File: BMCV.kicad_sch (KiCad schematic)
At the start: 30 parts, among them J13 DebugPins, J14 USB_C_Receptacle_USB2.0_14P, J17 ExpanderPort, SW14 Reset, SW15 Boot, U32 TXS0108EPW, U36 STM32G474CETx, Y1 38.4MHz 10pF

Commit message: rename symbol & footprint libs
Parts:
- J14: footprint MyParts:GT-USB-7035E -> BMCV:GT-USB-7035E
- SW14, SW15: footprint MyParts:TS-1095PS-AXXBX-C3DX -> BMCV:TS-1095PS-AXXBX-C3DX
- VR1: footprint MyParts:PTL6015xxxxxxx -> BMCV:PTL6015xxxxxxx; symbol MySymbols:PTLxx-xxxx-xxxxx -> BMCV:PTLxx-xxxx-xxxxx
- Z1: footprint MyParts:CataclystPanel -> BMCV:CataclystPanel; symbol MySymbols:FrontPanel -> BMCV:FrontPanel
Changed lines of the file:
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@@
 			)
 		)
-		(property "Footprint" "MyParts:TS-1095PS-AXXBX-C3DX"
+		(property "Footprint" "BMCV:TS-1095PS-AXXBX-C3DX"
 			(at 227.33 86.36 0)
 			(effects
@@
 	)
 	(symbol
-		(lib_id "MySymbols:PTLxx-xxxx-xxxxx")
+		(lib_id "BMCV:PTLxx-xxxx-xxxxx")
 		(at 59.69 189.23 0)
 		(unit 1)
@@
 			)
 		)
-		(property "Footprint" "MyParts:PTL6015xxxxxxx"
+		(property "Footprint" "BMCV:PTL6015xxxxxxx"
 			(at 88.9 284.15 0)
 			(effects
@@
 	)
 	(symbol
-		(lib_id "MySymbols:FrontPanel")
+		(lib_id "BMCV:FrontPanel")
 		(at 93.98 49.53 0)
 		(unit 1)
@@
 			)
 		)
-		(property "Footprint" "MyParts:CataclystPanel"
+		(property "Footprint" "BMCV:CataclystPanel"
 			(at 95.25 48.895 0)
 			(effects
@@
 			)
 		)
-		(property "Footprint" "MyParts:GT-USB-7035E"
+		(property "Footprint" "BMCV:GT-USB-7035E"
 			(at 41.91 102.87 0)
 			(effects
@@
 			)
 		)
-		(property "Footprint" "MyParts:TS-1095PS-AXXBX-C3DX"
+		(property "Footprint" "BMCV:TS-1095PS-AXXBX-C3DX"
 			(at 242.57 119.38 0)
 			(effects

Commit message: clea up project
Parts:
- Z1: footprint BMCV:CataclystPanel -> BMCV:BMCVPanel
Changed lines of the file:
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@@
 		)
 		(instances
-			(project "cataclyst"
+			(project "BMCV"
 				(path "/9b519346-c6ba-4bde-a176-1e9938a671fb"
 					(reference "C2")
@@
 		)
 		(instances
-			(project "cataclyst"
+			(project "BMCV"
 				(path "/9b519346-c6ba-4bde-a176-1e9938a671fb"
 					(reference "C6")
@@
 		)
 		(instances
-			(project "cataclyst"
+			(project "BMCV"
 				(path "/9b519346-c6ba-4bde-a176-1e9938a671fb"
 					(reference "C5")
@@
 		)
 		(instances
-			(project "cataclyst"
+			(project "BMCV"
 				(path "/9b519346-c6ba-4bde-a176-1e9938a671fb"
 					(reference "#PWR08")
@@
 		)
 		(instances
-			(project "cataclyst"
+			(project "BMCV"
 				(path "/9b519346-c6ba-4bde-a176-1e9938a671fb"
 					(reference "#PWR013")
@@
 		)
 		(instances
-			(project "cataclyst"
+			(project "BMCV"
 				(path "/9b519346-c6ba-4bde-a176-1e9938a671fb"
 					(reference "C46")
@@
 		)
 		(instances
-			(project "cataclyst"
+			(project "BMCV"
 				(path "/9b519346-c6ba-4bde-a176-1e9938a671fb"
 					(reference "#PWR0282")
@@
 		)
 		(instances
-			(project "cataclyst"
+			(project "BMCV"
 				(path "/9b519346-c6ba-4bde-a176-1e9938a671fb"
 					(reference "#PWR06")
@@
 		)
 		(instances
-			(project "cataclyst"
+			(project "BMCV"
 				(path "/9b519346-c6ba-4bde-a176-1e9938a671fb"
 					(reference "#PWR0284")
@@
 		)
 		(instances
-			(project "cataclyst"
+			(project "BMCV"
 				(path "/9b519346-c6ba-4bde-a176-1e9938a671fb"
 					(reference "#PWR029")
@@
 		)
 		(instances
-			(project "cataclyst"
+			(project "BMCV"
 				(path "/9b519346-c6ba-4bde-a176-1e9938a671fb"
 					(reference "C94")
@@
 			)
 		)
-		(property "Footprint" "BMCV:CataclystPanel"
+		(property "Footprint" "BMCV:BMCVPanel"
 			(at 95.25 48.895 0)
 			(effects
@@
 		)
 		(instances
-			(project "cataclyst"
+			(project "BMCV"
 				(path "/9b519346-c6ba-4bde-a176-1e9938a671fb"
 					(reference "#PWR030")
@@
 		)
 		(instances
-			(project "cataclyst"
+			(project "BMCV"
 				(path "/9b519346-c6ba-4bde-a176-1e9938a671fb"
 					(reference "#PWR0285")
@@
 		)
 		(instances
-			(project "cataclyst"
+			(project "BMCV"
 				(path "/9b519346-c6ba-4bde-a176-1e9938a671fb"
 					(reference "R163")
@@
 		)
 		(instances
-			(project "cataclyst"
+			(project "BMCV"
 				(path "/9b519346-c6ba-4bde-a176-1e9938a671fb"
 					(reference "C4")
@@
 		)
 		(instances
-			(project "cataclyst"
+			(project "BMCV"
 				(path "/9b519346-c6ba-4bde-a176-1e9938a671fb"
 					(reference "C7")
@@
 		)
 		(instances
-			(project "cataclyst"
+			(project "BMCV"
 				(path "/9b519346-c6ba-4bde-a176-1e9938a671fb"
 					(reference "R159")
@@
 		)
 		(instances
-			(project "cataclyst"
+			(project "BMCV"
 				(path "/9b519346-c6ba-4bde-a176-1e9938a671fb"
 					(reference "R2")
@@
 		)
 		(instances
-			(project "cataclyst"
+			(project "BMCV"
 				(path "/9b519346-c6ba-4bde-a176-1e9938a671fb"
 					(reference "C3")
@@
 		)
 		(instances
-			(project "cataclyst"
+			(project "BMCV"
 				(path "/9b519346-c6ba-4bde-a176-1e9938a671fb"
 					(reference "C93")
@@
 		)
 		(instances
-			(project "cataclyst"
+			(project "BMCV"
 				(path "/9b519346-c6ba-4bde-a176-1e9938a671fb"
 					(reference "R41")
@@
 		)
 		(instances
-			(project "cataclyst"
+			(project "BMCV"
 				(path "/9b519346-c6ba-4bde-a176-1e9938a671fb"
 					(reference "#PWR07")
@@
 		)
 		(instances
-			(project "cataclyst"
+			(project "BMCV"
 				(path "/9b519346-c6ba-4bde-a176-1e9938a671fb"
 					(reference "R162")
@@
 		)
 		(instances
-			(project "cataclyst"
+			(project "BMCV"
 				(path "/9b519346-c6ba-4bde-a176-1e9938a671fb"
 					(reference "#PWR0281")
@@
 		)
 		(instances
-			(project "cataclyst"
+			(project "BMCV"
 				(path "/9b519346-c6ba-4bde-a176-1e9938a671fb"
 					(reference "R161")
@@
 		)
 		(instances
-			(project "cataclyst"
+			(project "BMCV"
 				(path "/9b519346-c6ba-4bde-a176-1e9938a671fb"
 					(reference "#PWR014")
@@
 		)
 		(instances
-			(project "cataclyst"
+			(project "BMCV"
 				(path "/9b519346-c6ba-4bde-a176-1e9938a671fb"
 					(reference "#PWR028")
@@
 		)
 		(instances
-			(project "cataclyst"
+			(project "BMCV"
 				(path "/9b519346-c6ba-4bde-a176-1e9938a671fb"
 					(reference "#PWR0235")
@@
 		)
 		(instances
-			(project "cataclyst"
+			(project "BMCV"
 				(path "/9b519346-c6ba-4bde-a176-1e9938a671fb"
 					(reference "#PWR0279")
@@
 		)
 		(instances
-			(project "cataclyst"
+			(project "BMCV"
 				(path "/9b519346-c6ba-4bde-a176-1e9938a671fb"
 					(reference "#PWR015")
@@
 		)
 		(instances
-			(project "cataclyst"
+			(project "BMCV"
 				(path "/9b519346-c6ba-4bde-a176-1e9938a671fb"
 					(reference "#PWR0283")
@@
 		)
 		(instances
-			(project "cataclyst"
+			(project "BMCV"
 				(path "/9b519346-c6ba-4bde-a176-1e9938a671fb"
 					(reference "#PWR031")
@@
 		)
 		(instances
-			(project "cataclyst"
+			(project "BMCV"
 				(path "/9b519346-c6ba-4bde-a176-1e9938a671fb"
 					(reference "#PWR02")
@@
 		)
 		(instances
-			(project "cataclyst"
+			(project "BMCV"
 				(path "/9b519346-c6ba-4bde-a176-1e9938a671fb"
 					(reference "C11")
@@
 		)
 		(instances
-			(project "cataclyst"
+			(project "BMCV"
 				(path "/9b519346-c6ba-4bde-a176-1e9938a671fb"
 					(reference "#PWR0286")
@@
 		)
 		(instances
-			(project "cataclyst"
+			(project "BMCV"
 				(path "/9b519346-c6ba-4bde-a176-1e9938a671fb"
 					(reference "SW15")
@@
 		)
 		(instances
-			(project "cataclyst"
+			(project "BMCV"
 				(path "/9b519346-c6ba-4bde-a176-1e9938a671fb"
 					(reference "R158")
@@
 		)
 		(instances
-			(project "cataclyst"
+			(project "BMCV"
 				(path "/9b519346-c6ba-4bde-a176-1e9938a671fb"
 					(reference "#PWR0280")
@@
 		)
 		(instances
-			(project "cataclyst"
+			(project "BMCV"
 				(path "/9b519346-c6ba-4bde-a176-1e9938a671fb"
 					(reference "R3")
@@
 		)
 		(instances
-			(project "cataclyst"
+			(project "BMCV"
 				(path "/9b519346-c6ba-4bde-a176-1e9938a671fb"
 					(reference "#PWR0278")
@@
 		)
 		(instances
-			(project "cataclyst"
+			(project "BMCV"
 				(path "/9b519346-c6ba-4bde-a176-1e9938a671fb"
 					(reference "#PWR0268")
@@
 		)
 		(instances
-			(project "cataclyst"
+			(project "BMCV"
 				(path "/9b519346-c6ba-4bde-a176-1e9938a671fb"
 					(page "5")
@@
 		)
 		(instances
-			(project "cataclyst"
+			(project "BMCV"
 				(path "/9b519346-c6ba-4bde-a176-1e9938a671fb"
 					(page "6")
@@
 		)
 		(instances
-			(project "cataclyst"
+			(project "BMCV"
 				(path "/9b519346-c6ba-4bde-a176-1e9938a671fb"
 					(page "3")
@@
 		)
 		(instances
-			(project "cataclyst"
+			(project "BMCV"
 				(path "/9b519346-c6ba-4bde-a176-1e9938a671fb"
 					(page "4")
@@
 		)
 		(instances
-			(project "cataclyst"
+			(project "BMCV"
 				(path "/9b519346-c6ba-4bde-a176-1e9938a671fb"
 					(page "2")

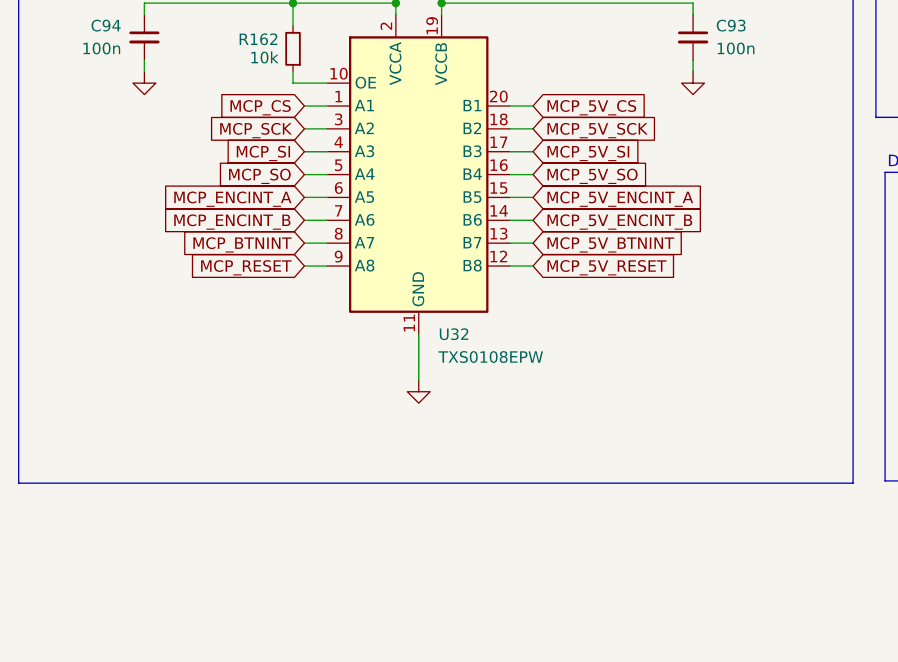
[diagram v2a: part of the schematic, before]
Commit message: routing progress (bottom buttons & encoders)
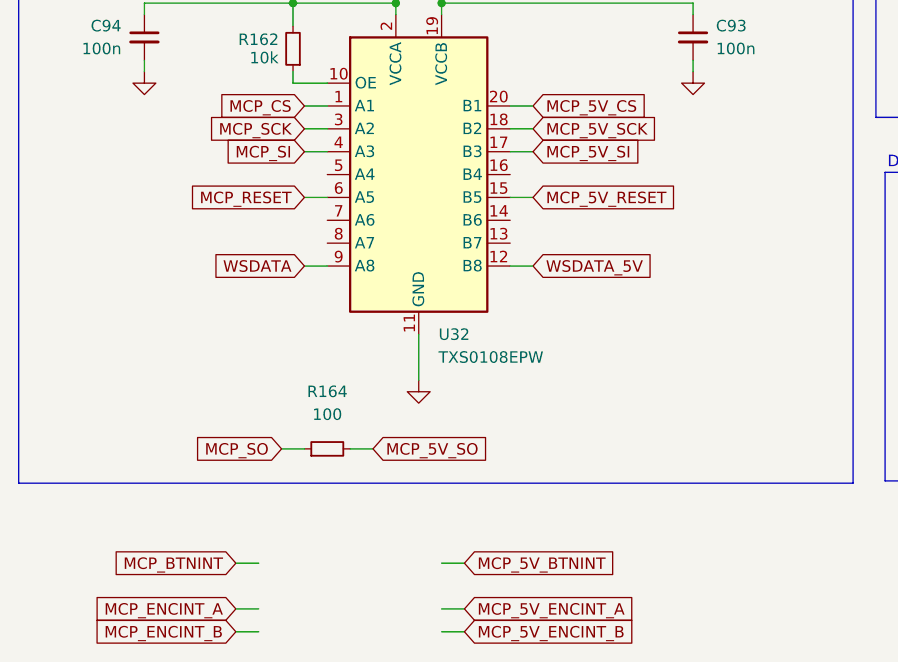
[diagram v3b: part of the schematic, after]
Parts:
- added R164: 100, Resistor_SMD:R_0603_1608Metric, symbol Device:R_Small
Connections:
- net MCP_5V_BTNINT: no longer U32.13 (B7)
- net MCP_5V_ENCINT_A: no longer U32.15 (B5)
- net MCP_5V_ENCINT_B: no longer U32.14 (B6)
- net MCP_5V_RESET: now also U32.15 (B5); no longer U32.12 (B8)
- net MCP_5V_SO: now also R164.2; no longer U32.16 (B4)
- net MCP_BTNINT: no longer U32.8 (A7)
- net MCP_ENCINT_A: no longer U32.6 (A5)
- net MCP_ENCINT_B: no longer U32.7 (A6)
- net MCP_RESET: now also U32.6 (A5); no longer U32.9 (A8)
- net MCP_SO: now also R164.1; no longer U32.5 (A4)
- new net WSDATA: U32.9 (A8)
- new net WSDATA_5V: U32.12 (B8)
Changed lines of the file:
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@@
 	(wire
 		(pts
-			(xy 69.85 247.65) (xy 72.39 247.65)
+			(xy 69.85 245.11) (xy 72.39 245.11)
 		)
 		(stroke
@@
 	(wire
 		(pts
-			(xy 69.85 245.11) (xy 72.39 245.11)
+			(xy 52.07 278.13) (xy 54.61 278.13)
 		)
 		(stroke
@@
 	(wire
 		(pts
-			(xy 69.85 252.73) (xy 72.39 252.73)
+			(xy 69.85 250.19) (xy 72.39 250.19)
 		)
 		(stroke
@@
 	(wire
 		(pts
-			(xy 46.99 252.73) (xy 49.53 252.73)
+			(xy 39.37 295.91) (xy 41.91 295.91)
 		)
 		(stroke
@@
 	(wire
 		(pts
-			(xy 46.99 255.27) (xy 49.53 255.27)
+			(xy 39.37 298.45) (xy 41.91 298.45)
 		)
 		(stroke
@@
 	(wire
 		(pts
-			(xy 46.99 247.65) (xy 49.53 247.65)
+			(xy 39.37 290.83) (xy 41.91 290.83)
 		)
 		(stroke
@@
 	(wire
 		(pts
-			(xy 69.85 250.19) (xy 72.39 250.19)
+			(xy 62.23 290.83) (xy 64.77 290.83)
 		)
 		(stroke
@@
 	(wire
 		(pts
+			(xy 46.99 245.11) (xy 49.53 245.11)
+		)
+		(stroke
+			(width 0)
+			(type default)
+		)
+	)
+	(wire
+		(pts
 			(xy 265.43 124.46) (xy 267.97 124.46)
 		)
@@
 	(wire
 		(pts
-			(xy 69.85 255.27) (xy 72.39 255.27)
+			(xy 62.23 295.91) (xy 64.77 295.91)
 		)
 		(stroke
@@
 	(wire
 		(pts
+			(xy 69.85 257.81) (xy 72.39 257.81)
+		)
+		(stroke
+			(width 0)
+			(type default)
+		)
+	)
+	(wire
+		(pts
 			(xy 80.01 161.29) (xy 80.01 153.67)
 		)
@@
 	(wire
 		(pts
-			(xy 69.85 257.81) (xy 72.39 257.81)
+			(xy 62.23 298.45) (xy 64.77 298.45)
 		)
 		(stroke
@@
 	(wire
 		(pts
-			(xy 46.99 245.11) (xy 49.53 245.11)
+			(xy 44.45 278.13) (xy 46.99 278.13)
 		)
 		(stroke
@@
 	(global_label "MCP_SO"
 		(shape input)
-		(at 46.99 247.65 180)
+		(at 44.45 278.13 180)
 		(fields_autoplaced yes)
 		(effects
@@
 		)
 		(property "Intersheetrefs" "${INTERSHEET_REFS}"
-			(at 36.5058 247.65 0)
+			(at 33.9658 278.13 0)
 			(effects
 				(font
@@
 		)
 	)
+	(global_label "WSDATA"
+		(shape input)
+		(at 46.99 257.81 180)
+		(fields_autoplaced yes)
+		(effects
+			(font
+				(size 1.27 1.27)
+			)
+			(justify right)
+		)
+		(property "Intersheetrefs" "${INTERSHEET_REFS}"
+			(at 36.9291 257.81 0)
+			(effects
+				(font
+					(size 1.27 1.27)
+				)
+				(justify right)
+				(hide yes)
+			)
+		)
+	)
 	(global_label "ADC_ADDR"
 		(shape input)
@@
 	(global_label "MCP_5V_ENCINT_A"
 		(shape input)
-		(at 72.39 250.19 0)
+		(at 64.77 295.91 0)
 		(fields_autoplaced yes)
 		(effects
@@
 		)
 		(property "Intersheetrefs" "${INTERSHEET_REFS}"
-			(at 92.3085 250.19 0)
+			(at 84.6885 295.91 0)
 			(effects
 				(font
@@
 	(global_label "MCP_RESET"
 		(shape input)
-		(at 46.99 257.81 180)
+		(at 46.99 250.19 180)
 		(fields_autoplaced yes)
 		(effects
@@
 		)
 		(property "Intersheetrefs" "${INTERSHEET_REFS}"
-			(at 33.3007 257.81 0)
+			(at 33.3007 250.19 0)
 			(effects
 				(font
@@
 	(global_label "MCP_5V_BTNINT"
 		(shape input)
-		(at 72.39 255.27 0)
+		(at 64.77 290.83 0)
 		(fields_autoplaced yes)
 		(effects
@@
 		)
 		(property "Intersheetrefs" "${INTERSHEET_REFS}"
-			(at 90.0709 255.27 0)
+			(at 82.4509 290.83 0)
 			(effects
 				(font
@@
 	(global_label "MCP_5V_SO"
 		(shape input)
-		(at 72.39 247.65 0)
+		(at 54.61 278.13 0)
 		(fields_autoplaced yes)
 		(effects
@@
 		)
 		(property "Intersheetrefs" "${INTERSHEET_REFS}"
-			(at 86.1399 247.65 0)
+			(at 68.3599 278.13 0)
 			(effects
 				(font
@@
 	(global_label "MCP_5V_RESET"
 		(shape input)
+		(at 72.39 250.19 0)
+		(fields_autoplaced yes)
+		(effects
+			(font
+				(size 1.27 1.27)
+			)
+			(justify left)
+		)
+		(property "Intersheetrefs" "${INTERSHEET_REFS}"
+			(at 89.345 250.19 0)
+			(effects
+				(font
+					(size 1.27 1.27)
+				)
+				(justify left)
+				(hide yes)
+			)
+		)
+	)
+	(global_label "WSDATA_5V"
+		(shape input)
 		(at 72.39 257.81 0)
 		(fields_autoplaced yes)
@@
 		)
 		(property "Intersheetrefs" "${INTERSHEET_REFS}"
-			(at 89.345 257.81 0)
+			(at 85.7166 257.81 0)
 			(effects
 				(font
@@
 	(global_label "MCP_BTNINT"
 		(shape input)
-		(at 46.99 255.27 180)
+		(at 39.37 290.83 180)
 		(fields_autoplaced yes)
 		(effects
@@
 		)
 		(property "Intersheetrefs" "${INTERSHEET_REFS}"
-			(at 32.5748 255.27 0)
+			(at 24.9548 290.83 0)
 			(effects
 				(font
@@
 	(global_label "MCP_ENCINT_B"
 		(shape input)
-		(at 46.99 252.73 180)
+		(at 39.37 298.45 180)
 		(fields_autoplaced yes)
 		(effects
@@
 		)
 		(property "Intersheetrefs" "${INTERSHEET_REFS}"
-			(at 30.1558 252.73 0)
+			(at 22.5358 298.45 0)
 			(effects
 				(font
@@
 	(global_label "MCP_5V_ENCINT_B"
 		(shape input)
-		(at 72.39 252.73 0)
+		(at 64.77 298.45 0)
 		(fields_autoplaced yes)
 		(effects
@@
 		)
 		(property "Intersheetrefs" "${INTERSHEET_REFS}"
-			(at 92.4899 252.73 0)
+			(at 84.8699 298.45 0)
 			(effects
 				(font
@@
 	(global_label "MCP_ENCINT_A"
 		(shape input)
-		(at 46.99 250.19 180)
+		(at 39.37 295.91 180)
 		(fields_autoplaced yes)
 		(effects
@@
 		)
 		(property "Intersheetrefs" "${INTERSHEET_REFS}"
-			(at 30.3372 250.19 0)
+			(at 22.7172 295.91 0)
 			(effects
 				(font
@@
 					(unit 1)
 				)
+			)
+		)
+	)
+	(symbol
+		(lib_id "Device:R_Small")
+		(at 49.53 278.13 90)
+		(unit 1)
+		(exclude_from_sim no)
+		(in_bom yes)
+		(on_board yes)
+		(dnp no)
+		(property "Reference" "R164"
+			(at 49.53 271.78 90)
+			(effects
+				(font
+					(size 1.27 1.27)
+				)
+			)
+		)
+		(property "Value" "100"
+			(at 49.53 274.32 90)
+			(effects
+				(font
+					(size 1.27 1.27)
+				)
+			)
+		)
+		(property "Footprint" "Resistor_SMD:R_0603_1608Metric"
+			(at 49.53 278.13 0)
+			(effects
+				(font
+					(size 1.27 1.27)
+				)
+				(hide yes)
+			)
+		)
+		(property "Datasheet" "~"
+			(at 49.53 278.13 0)
+			(effects
+				(font
+					(size 1.27 1.27)
+				)
+				(hide yes)
+			)
+		)
+		(property "Description" "Resistor, small symbol"
+			(at 49.53 278.13 0)
+			(effects
+				(font
+					(size 1.27 1.27)
+				)
+				(hide yes)
+			)
+		)
+		(pin "2"
+		)
+		(pin "1"
+		)
+		(instances
+			(project "BMCV"
+				(path "/9b519346-c6ba-4bde-a176-1e9938a671fb"
+					(reference "R164")
+					(unit 1)
+				)

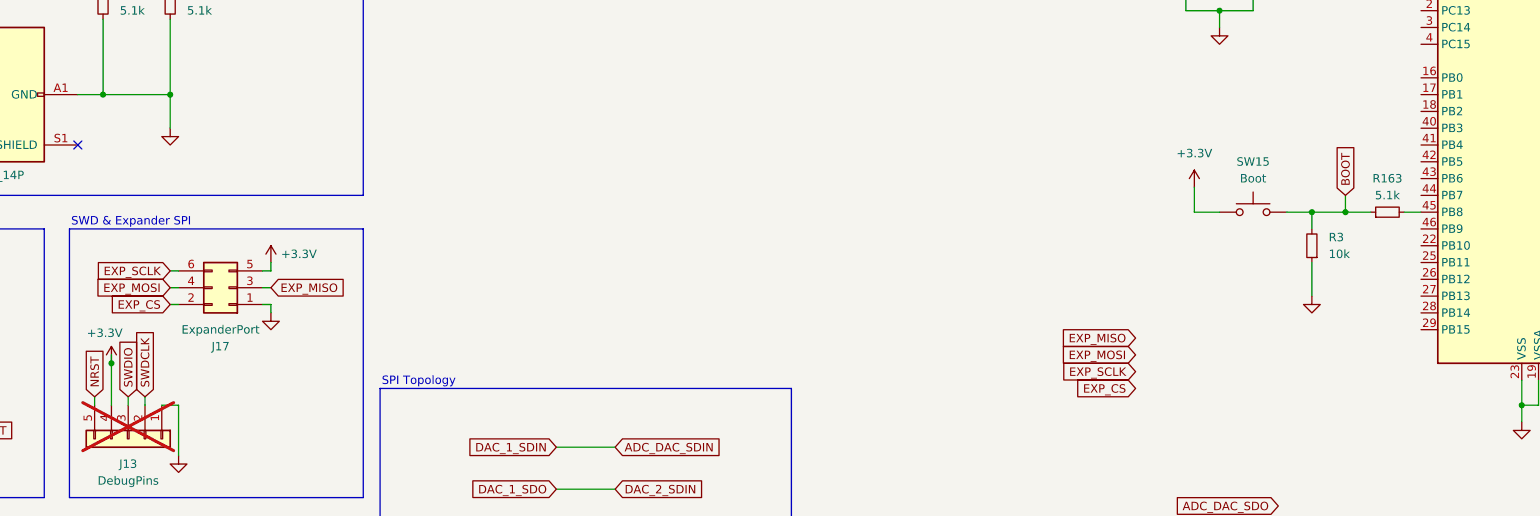
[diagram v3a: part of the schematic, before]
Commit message: remove expander for now, update model/move usb
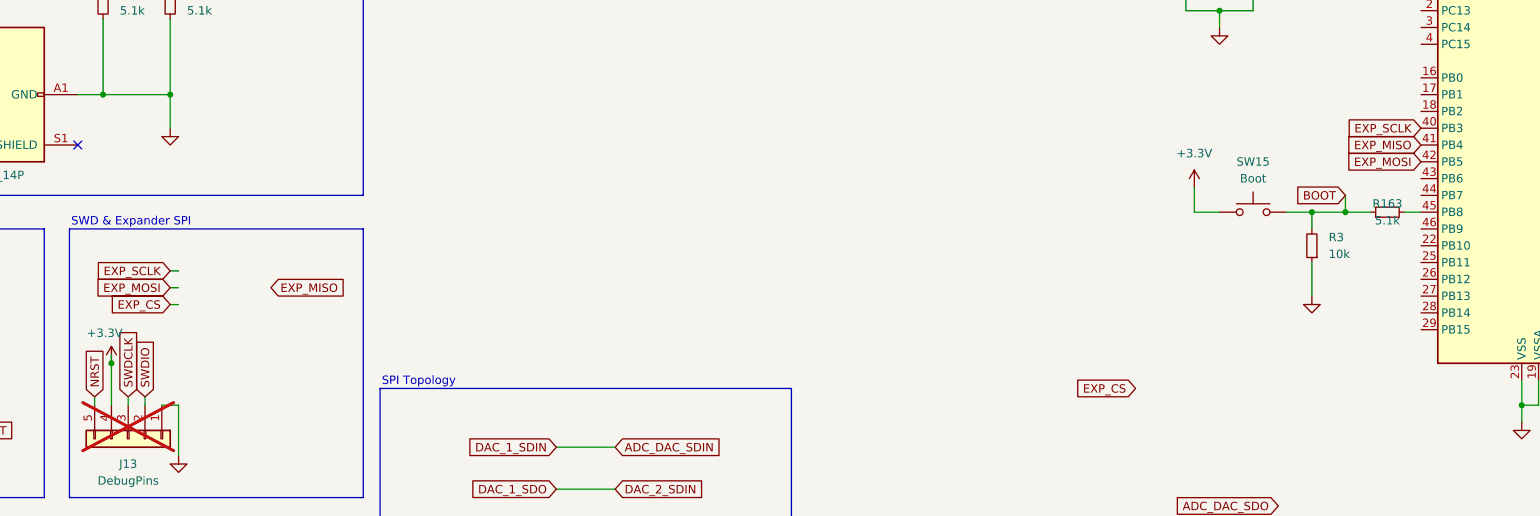
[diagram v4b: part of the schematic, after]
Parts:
- removed J17: ExpanderPort, Connector_IDC:IDC-Header_2x03_P2.54mm_Vertical, symbol Connector_Generic:Conn_02x03_Odd_Even
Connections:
- net EXP_MISO: now also U36.41 (PB4)
- net EXP_MOSI: now also U36.42 (PB5)
- net EXP_SCLK: now also U36.40 (PB3)
- net SWDCLK: now also J13.3 (Pin_3); no longer J13.2 (Pin_2)
- net SWDIO: now also J13.2 (Pin_2); no longer J13.3 (Pin_3)
